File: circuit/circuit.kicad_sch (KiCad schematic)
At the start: 21 parts, among them J5 PWR1, J6 Signal1, J7 PWR2, J8 Signal2, Q3 BC337, U5 ADuM1250, U6 Optocoupler_DC_PhotoNPN_AKEC, U7 LM7805

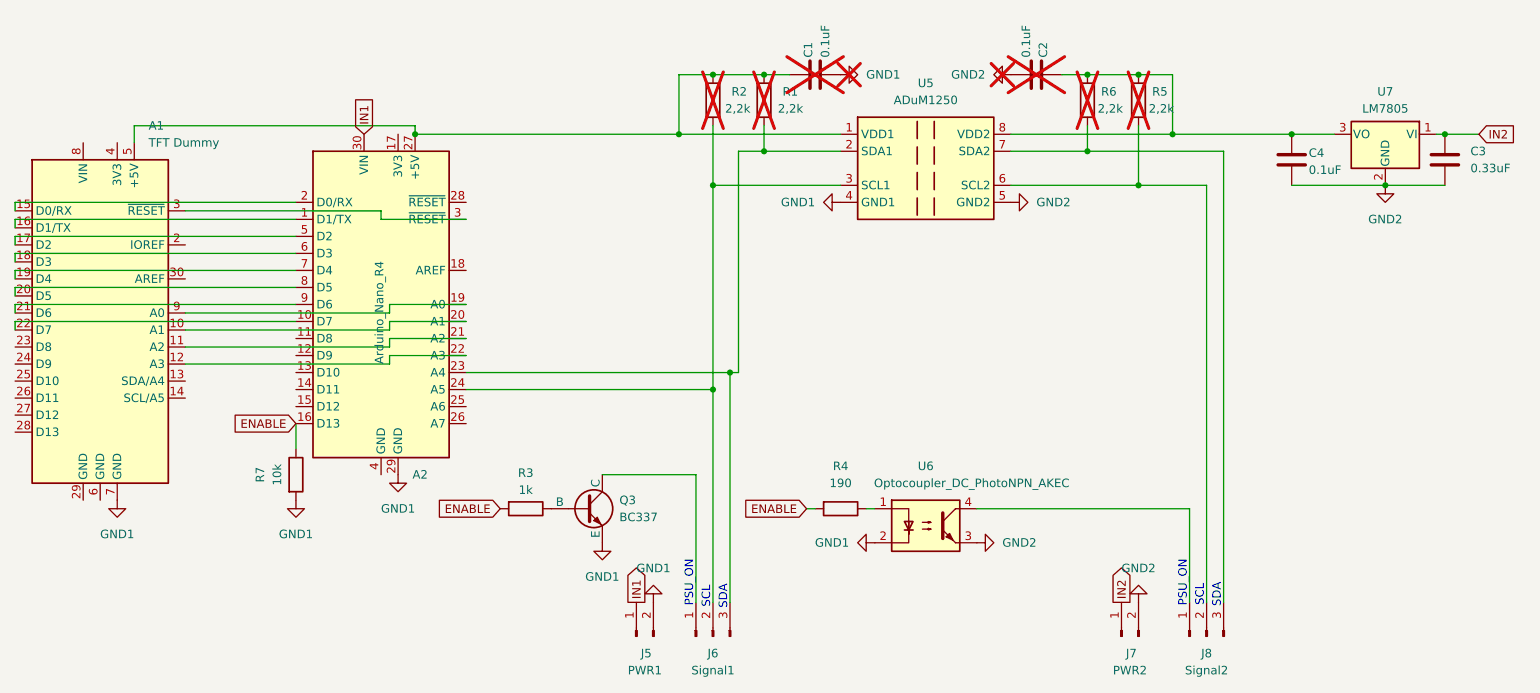
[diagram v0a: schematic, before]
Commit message: Updated PCB layout and circuit.
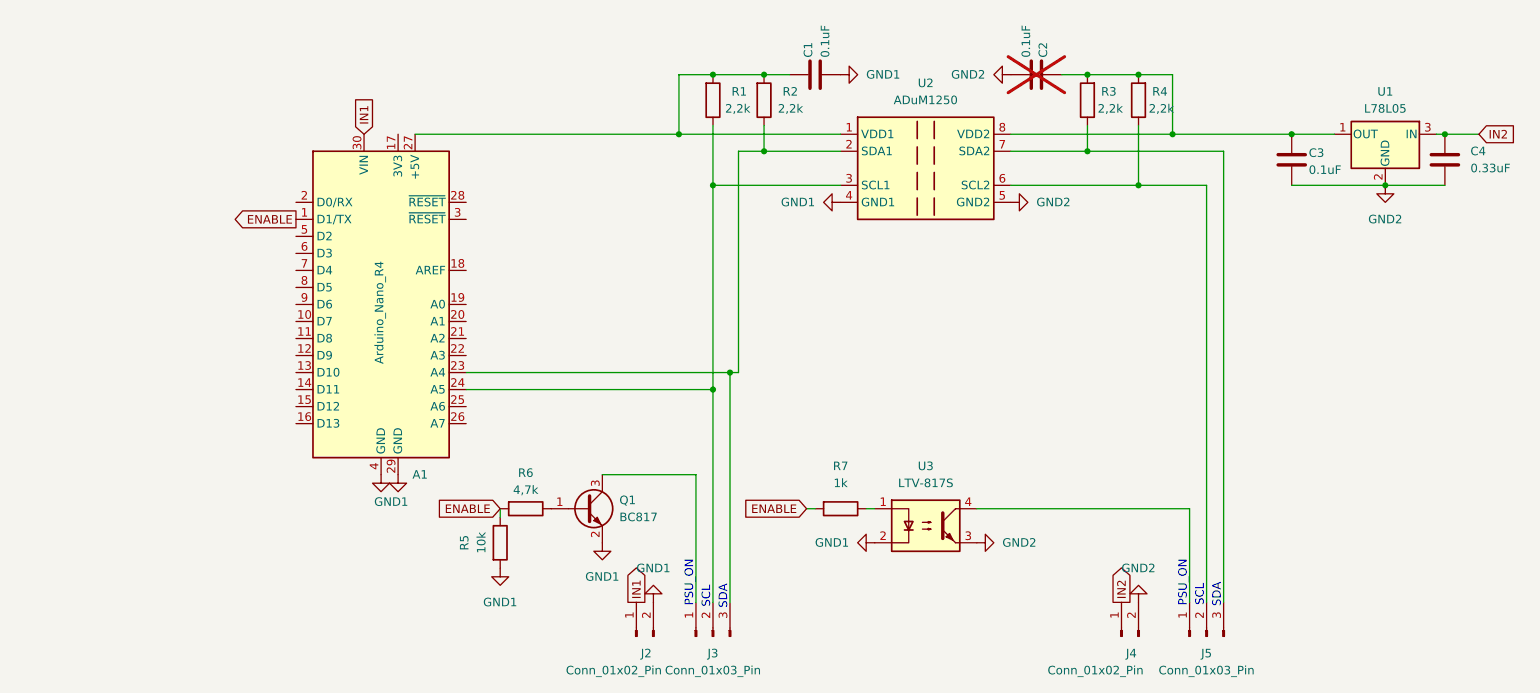
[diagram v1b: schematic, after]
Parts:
- removed A1: TFT Dummy, Module:Arduino_UNO_R2, symbol MCU_Module:Arduino_UNO_R2
- removed Q3: BC337, Package_TO_SOT_THT:TO-92, symbol Simulation_SPICE:NPN
- removed U6: Optocoupler_DC_PhotoNPN_AKEC, Package_DIP:DIP-4_W7.62mm_SMDSocket_SmallPads, symbol Isolator:Optocoupler_DC_PhotoNPN_AKEC
- added Q1: BC817, Package_TO_SOT_SMD:SOT-23, symbol Transistor_BJT:BC817
- added U3: LTV-817S, Package_DIP:SMDIP-4_W9.53mm, symbol Isolator:LTV-817S
- A1: renamed from A2; now left out of the parts list
- C1: footprint (none) -> Capacitor_SMD:C_0603_1608Metric; LCSC (none) -> C125205; now fitted; now in the parts list
- C2: footprint (none) -> Capacitor_SMD:C_0603_1608Metric
- C3: renamed from C4; footprint Capacitor_SMD:C_0201_0603Metric -> Capacitor_SMD:C_0603_1608Metric; LCSC (none) -> C125205
- C4: renamed from C3; footprint Capacitor_SMD:C_0201_0603Metric -> Capacitor_SMD:C_0603_1608Metric; LCSC (none) -> C107070
- J2: renamed from J5; value PWR1 -> Conn_01x02_Pin; LCSC (none) -> C492401
- J3: renamed from J6; value Signal1 -> Conn_01x03_Pin; LCSC (none) -> C2937625
- J4: renamed from J7; value PWR2 -> Conn_01x02_Pin; LCSC (none) -> C492401
- J5: renamed from J8; value Signal2 -> Conn_01x03_Pin; LCSC (none) -> C2937625
- R1: renamed from R2; footprint (none) -> Resistor_SMD:R_0603_1608Metric; LCSC (none) -> C114662; now fitted; now in the parts list
- R2: renamed from R1; footprint (none) -> Resistor_SMD:R_0603_1608Metric; LCSC (none) -> C114662; now fitted; now in the parts list
- R3: renamed from R6; footprint (none) -> Resistor_SMD:R_0603_1608Metric; LCSC (none) -> C114662; now fitted; now in the parts list
- R4: renamed from R5; footprint (none) -> Resistor_SMD:R_0603_1608Metric; LCSC (none) -> C114662; now fitted; now in the parts list
- R5: renamed from R7; footprint Resistor_SMD:R_0201_0603Metric -> Resistor_SMD:R_0603_1608Metric; LCSC (none) -> C98220
- R6: renamed from R3; value 1k -> 4,7k; footprint Resistor_SMD:R_0201_0603Metric -> Resistor_SMD:R_0603_1608Metric; LCSC (none) -> C99782
- R7: renamed from R4; value 190 -> 1k; footprint Resistor_SMD:R_0201_0603Metric -> Resistor_SMD:R_0603_1608Metric; LCSC (none) -> C22548
- U1: renamed from U7; value LM7805 -> L78L05; footprint Package_TO_SOT_SMD:SOT-223-3_TabPin2 -> Package_TO_SOT_SMD:SOT-89-3; symbol Regulator_Linear:LM7805_TO220 -> Regulator_Linear:L78L05_SOT89; LCSC (none) -> C42738
- U2: renamed from U5; LCSC (none) -> C579378
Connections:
- net ENABLE: now also A1.1 (D1/TX); no longer A1.16 (D13)
- net GND1: now also A1.4 (GND), Q1.2 (E), U3.2
- net GND2: now also U3.3
- net IN2: now also U1.3 (IN); no longer U1.1 (VI)
- net at C2.1, C3.1, R3.2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: now also U1.1 (OUT); no longer U1.3 (VO)
- net at R7.1: now also U3.1
- net at R6.1: now also Q1.1 (B)
- net at J5.1 (Pin_1): now also U3.4
- net at J3.1 (Pin_1): now also Q1.3 (C)
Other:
- moved on the sheet: R5
